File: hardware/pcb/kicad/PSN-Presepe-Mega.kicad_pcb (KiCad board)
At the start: 2 copper layers, 280 x 170 mm, 77 parts, among them J1 12V_IN, K1 G5Q-1_DC12, K10 G5Q-1_DC12, K11 G5Q-1_DC12, K12 G5Q-1_DC12, K13 G5Q-1_DC12, K14 G5Q-1_DC12, K15 G5Q-1_DC12, K16 G5Q-1_DC12, K2 G5Q-1_DC12, K3 G5Q-1_DC12, K4 G5Q-1_DC12, K5 G5Q-1_DC12, K6 G5Q-1_DC12, K7 G5Q-1_DC12, K8 G5Q-1_DC12, K9 G5Q-1_DC12, Q1 IRLZ44N_CIELO_R, Q2 IRLZ44N_CIELO_G, Q3 IRLZ44N_CIELO_B, Q4 IRLZ44N_TRAM_R, Q5 IRLZ44N_TRAM_G, Q6 IRLZ44N_TRAM_B, Q7 IRLZ44N_ALBA_R, Q8 IRLZ44N_ALBA_G, Q9 IRLZ44N_ALBA_B, U1 ULN2803C, U2 ULN2803C

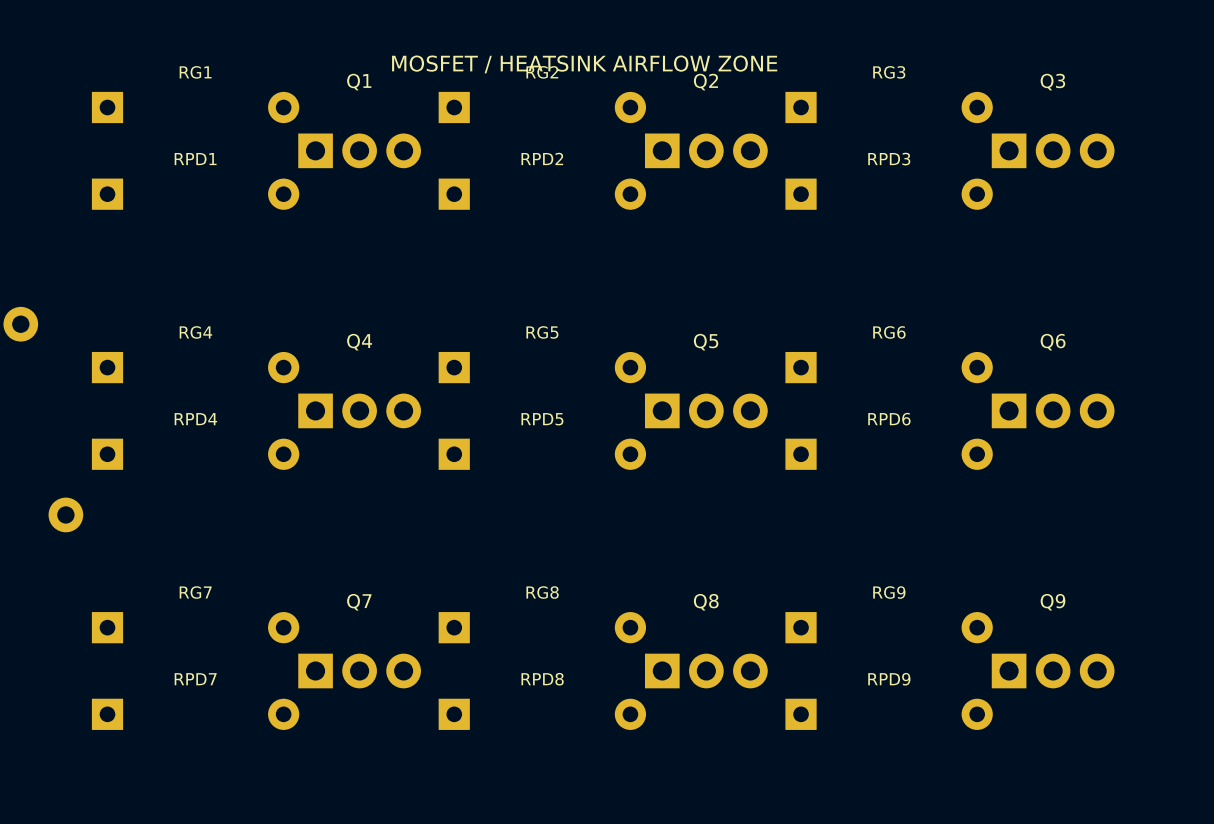
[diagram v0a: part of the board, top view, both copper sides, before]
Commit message: Route validated local MOSFET gate and ground network
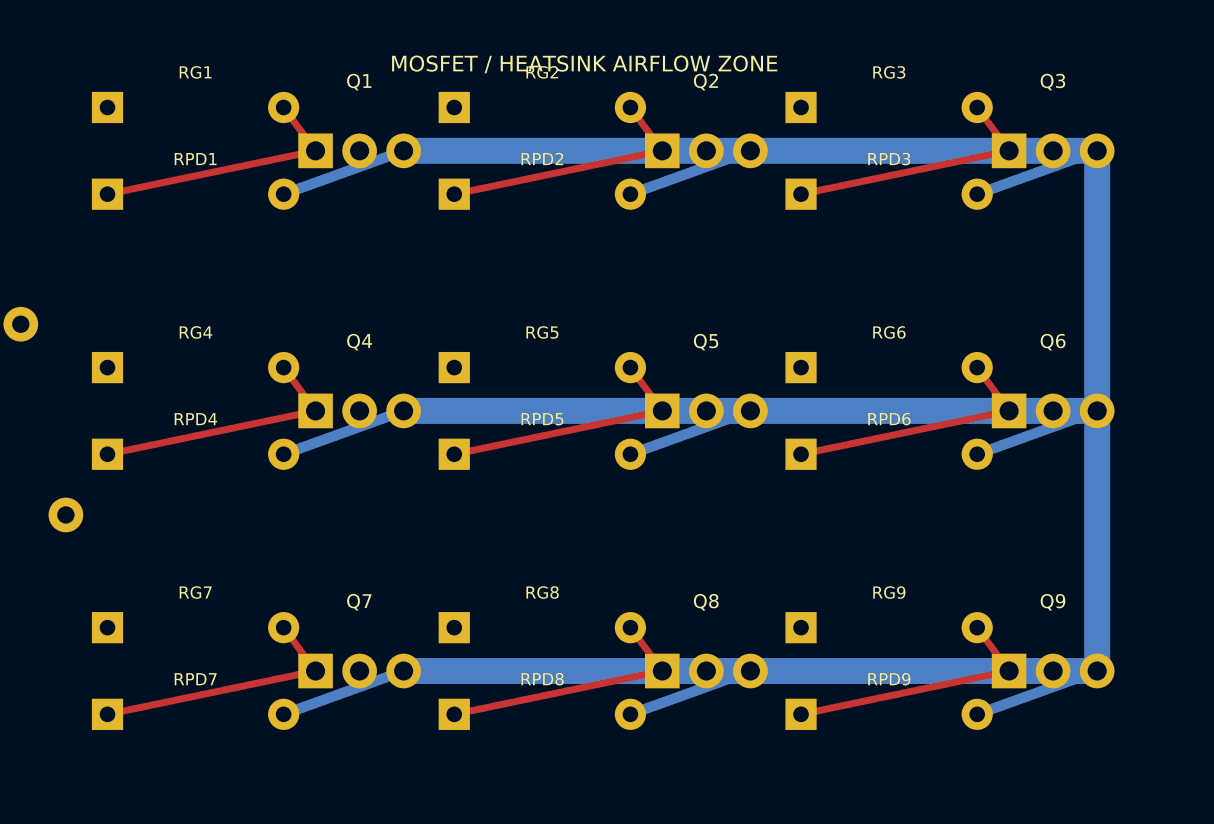
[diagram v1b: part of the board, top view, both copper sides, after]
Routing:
- net GND: track 0.00 -> 216.2 mm
- net GATE_Q9: track 0.00 -> 15.4 mm
- net GATE_Q8: track 0.00 -> 15.4 mm
- net GATE_Q7: track 0.00 -> 15.4 mm
- net GATE_Q6: track 0.00 -> 15.4 mm
- net GATE_Q5: track 0.00 -> 15.4 mm
- net GATE_Q4: track 0.00 -> 15.4 mm
- net GATE_Q3: track 0.00 -> 15.4 mm
- net GATE_Q2: track 0.00 -> 15.4 mm
- net GATE_Q1: track 0.00 -> 15.4 mm
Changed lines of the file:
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@@
   (gr_text "ALL TERMINAL WIRE ENTRY OUTWARD" (at 160 188) (layer "F.SilkS") (effects (font (size 0.9 0.9) (thickness 0.16))))
   (gr_text "MOSFET / HEATSINK AIRFLOW ZONE" (at 85.5 130) (layer "F.SilkS") (effects (font (size 0.9 0.9) (thickness 0.16))))
+  (segment (start 68.16 132.5) (end 70 135) (width 0.4) (layer "F.Cu") (net 63))
+  (segment (start 70 135) (end 58 137.5) (width 0.4) (layer "F.Cu") (net 63))
+  (segment (start 68.16 137.5) (end 75.08 135) (width 0.6) (layer "B.Cu") (net 1))
+  (segment (start 88.16 132.5) (end 90 135) (width 0.4) (layer "F.Cu") (net 64))
+  (segment (start 90 135) (end 78 137.5) (width 0.4) (layer "F.Cu") (net 64))
+  (segment (start 88.16 137.5) (end 95.08 135) (width 0.6) (layer "B.Cu") (net 1))
+  (segment (start 108.16 132.5) (end 110 135) (width 0.4) (layer "F.Cu") (net 65))
+  (segment (start 110 135) (end 98 137.5) (width 0.4) (layer "F.Cu") (net 65))
+  (segment (start 108.16 137.5) (end 115.08 135) (width 0.6) (layer "B.Cu") (net 1))
+  (segment (start 68.16 147.5) (end 70 150) (width 0.4) (layer "F.Cu") (net 66))
+  (segment (start 70 150) (end 58 152.5) (width 0.4) (layer "F.Cu") (net 66))
+  (segment (start 68.16 152.5) (end 75.08 150) (width 0.6) (layer "B.Cu") (net 1))
+  (segment (start 88.16 147.5) (end 90 150) (width 0.4) (layer "F.Cu") (net 67))
+  (segment (start 90 150) (end 78 152.5) (width 0.4) (layer "F.Cu") (net 67))
+  (segment (start 88.16 152.5) (end 95.08 150) (width 0.6) (layer "B.Cu") (net 1))
+  (segment (start 108.16 147.5) (end 110 150) (width 0.4) (layer "F.Cu") (net 68))
+  (segment (start 110 150) (end 98 152.5) (width 0.4) (layer "F.Cu") (net 68))
+  (segment (start 108.16 152.5) (end 115.08 150) (width 0.6) (layer "B.Cu") (net 1))
+  (segment (start 68.16 162.5) (end 70 165) (width 0.4) (layer "F.Cu") (net 69))
+  (segment (start 70 165) (end 58 167.5) (width 0.4) (layer "F.Cu") (net 69))
+  (segment (start 68.16 167.5) (end 75.08 165) (width 0.6) (layer "B.Cu") (net 1))
+  (segment (start 88.16 162.5) (end 90 165) (width 0.4) (layer "F.Cu") (net 70))
+  (segment (start 90 165) (end 78 167.5) (width 0.4) (layer "F.Cu") (net 70))
+  (segment (start 88.16 167.5) (end 95.08 165) (width 0.6) (layer "B.Cu") (net 1))
+  (segment (start 108.16 162.5) (end 110 165) (width 0.4) (layer "F.Cu") (net 71))
+  (segment (start 110 165) (end 98 167.5) (width 0.4) (layer "F.Cu") (net 71))
+  (segment (start 108.16 167.5) (end 115.08 165) (width 0.6) (layer "B.Cu") (net 1))
+  (segment (start 75.08 135) (end 115.08 135) (width 1.5) (layer "B.Cu") (net 1))
+  (segment (start 75.08 150) (end 115.08 150) (width 1.5) (layer "B.Cu") (net 1))
+  (segment (start 75.08 165) (end 115.08 165) (width 1.5) (layer "B.Cu") (net 1))
+  (segment (start 115.08 135) (end 115.08 165) (width 1.5) (layer "B.Cu") (net 1))
 )

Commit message: Route 12V ground and relay coil power
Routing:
- net +12V: track 0.00 -> 555.1 mm
- net GND: track 216.2 -> 445.7 mm
- net RELAY16_COIL_LOW: track 0.00 -> 195.2 mm
- net RELAY8_COIL_LOW: track 0.00 -> 179.2 mm
- net RELAY15_COIL_LOW: track 0.00 -> 176.7 mm
- net RELAY7_COIL_LOW: track 0.00 -> 160.7 mm
- net RELAY14_COIL_LOW: track 0.00 -> 158.3 mm
- net RELAY6_COIL_LOW: track 0.00 -> 142.3 mm
- net RELAY13_COIL_LOW: track 0.00 -> 139.8 mm
- net RELAY5_COIL_LOW: track 0.00 -> 123.8 mm
- net RELAY12_COIL_LOW: track 0.00 -> 121.4 mm
- net RELAY4_COIL_LOW: track 0.00 -> 105.4 mm
- net RELAY11_COIL_LOW: track 0.00 -> 102.9 mm
- net RELAY3_COIL_LOW: track 0.00 -> 86.9 mm
- net RELAY10_COIL_LOW: track 0.00 -> 84.4 mm
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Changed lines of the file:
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@@
   (segment (start 75.08 165) (end 115.08 165) (width 1.5) (layer "B.Cu") (net 1))
   (segment (start 115.08 135) (end 115.08 165) (width 1.5) (layer "B.Cu") (net 1))
+  (segment (start 28 184) (end 28 120) (width 1.5) (layer "B.Cu") (net 2))
+  (segment (start 28 120) (end 73.72 120) (width 1.5) (layer "B.Cu") (net 2))
+  (segment (start 73.72 120) (end 73.72 89.46) (width 1.5) (layer "B.Cu") (net 2))
+  (segment (start 73.72 120) (end 126.16 120) (width 1.5) (layer "B.Cu") (net 2))
+  (segment (start 126.16 120) (end 126.16 112.32) (width 1.0) (layer "B.Cu") (net 2))
+  (segment (start 126.16 82.32) (end 126.16 112.32) (width 1.0) (layer "B.Cu") (net 2))
+  (segment (start 150 60) (end 276 60) (width 1.5) (layer "B.Cu") (net 2))
+  (segment (start 150 115) (end 276 115) (width 1.5) (layer "B.Cu") (net 2))
+  (segment (start 126.16 82.32) (end 134 82.32) (width 1.0) (layer "B.Cu") (net 2))
+  (segment (start 134 82.32) (end 134 60) (width 1.0) (layer "B.Cu") (net 2))
+  (segment (start 134 60) (end 150 60) (width 1.0) (layer "B.Cu") (net 2))
+  (segment (start 126.16 112.32) (end 134 112.32) (width 1.0) (layer "B.Cu") (net 2))
+  (segment (start 134 112.32) (end 134 115) (width 1.0) (layer "B.Cu") (net 2))
+  (segment (start 134 115) (end 150 115) (width 1.0) (layer "B.Cu") (net 2))
+  (segment (start 33.08 184) (end 33.08 176) (width 1.5) (layer "B.Cu") (net 1))
+  (segment (start 33.08 176) (end 120 176) (width 1.5) (layer "B.Cu") (net 1))
+  (segment (start 68.64 89.46) (end 68.64 118) (width 1.2) (layer "B.Cu") (net 1))
+  (segment (start 68.64 118) (end 120 118) (width 1.2) (layer "B.Cu") (net 1))
+  (segment (start 116 82.32) (end 120 82.32) (width 0.8) (layer "B.Cu") (net 1))
+  (segment (start 120 82.32) (end 120 118) (width 1.0) (layer "B.Cu") (net 1))
+  (segment (start 116 112.32) (end 120 112.32) (width 0.8) (layer "B.Cu") (net 1))
+  (segment (start 115.08 165) (end 115.08 176) (width 1.5) (layer "B.Cu") (net 1))
+  (segment (start 126.16 62) (end 130 62) (width 0.5) (layer "B.Cu") (net 36))
+  (segment (start 130 62) (end 130 85.5) (width 0.5) (layer "B.Cu") (net 36))
+  (segment (start 130 85.5) (end 142.38 85.5) (width 0.5) (layer "B.Cu") (net 36))
+  (segment (start 142.38 85.5) (end 142.38 75.24) (width 0.5) (layer "B.Cu") (net 36))
+  (segment (start 126.16 64.54) (end 130 64.54) (width 0.5) (layer "B.Cu") (net 37))
+  (segment (start 130 64.54) (end 130 87) (width 0.5) (layer "B.Cu") (net 37))
+  (segment (start 130 87) (end 160.38 87) (width 0.5) (layer "B.Cu") (net 37))
+  (segment (start 160.38 87) (end 160.38 75.24) (width 0.5) (layer "B.Cu") (net 37))
+  (segment (start 126.16 67.08) (end 130 67.08) (width 0.5) (layer "B.Cu") (net 38))
+  (segment (start 130 67.08) (end 130 88.5) (width 0.5) (layer "B.Cu") (net 38))
+  (segment (start 130 88.5) (end 178.38 88.5) (width 0.5) (layer "B.Cu") (net 38))
+  (segment (start 178.38 88.5) (end 178.38 75.24) (width 0.5) (layer "B.Cu") (net 38))
+  (segment (start 126.16 69.62) (end 130 69.62) (width 0.5) (layer "B.Cu") (net 39))
+  (segment (start 130 69.62) (end 130 90) (width 0.5) (layer "B.Cu") (net 39))
+  (segment (start 130 90) (end 196.38 90) (width 0.5) (layer "B.Cu") (net 39))
+  (segment (start 196.38 90) (end 196.38 75.24) (width 0.5) (layer "B.Cu") (net 39))
+  (segment (start 126.16 72.16) (end 130 72.16) (width 0.5) (layer "B.Cu") (net 40))
+  (segment (start 130 72.16) (end 130 91.5) (width 0.5) (layer "B.Cu") (net 40))
+  (segment (start 130 91.5) (end 214.38 91.5) (width 0.5) (layer "B.Cu") (net 40))
+  (segment (start 214.38 91.5) (end 214.38 75.24) (width 0.5) (layer "B.Cu") (net 40))
+  (segment (start 126.16 74.7) (end 130 74.7) (width 0.5) (layer "B.Cu") (net 41))
+  (segment (start 130 74.7) (end 130 93) (width 0.5) (layer "B.Cu") (net 41))
+  (segment (start 130 93) (end 232.38 93) (width 0.5) (layer "B.Cu") (net 41))
+  (segment (start 232.38 93) (end 232.38 75.24) (width 0.5) (layer "B.Cu") (net 41))
+  (segment (start 126.16 77.24) (end 130 77.24) (width 0.5) (layer "B.Cu") (net 42))
+  (segment (start 130 77.24) (end 130 94.5) (width 0.5) (layer "B.Cu") (net 42))
+  (segment (start 130 94.5) (end 250.38 94.5) (width 0.5) (layer "B.Cu") (net 42))
+  (segment (start 250.38 94.5) (end 250.38 75.24) (width 0.5) (layer "B.Cu") (net 42))
+  (segment (start 126.16 79.78) (end 130 79.78) (width 0.5) (layer "B.Cu") (net 43))
+  (segment (start 130 79.78) (end 130 96) (width 0.5) (layer "B.Cu") (net 43))
+  (segment (start 130 96) (end 268.38 96) (width 0.5) (layer "B.Cu") (net 43))
+  (segment (start 268.38 96) (end 268.38 75.24) (width 0.5) (layer "B.Cu") (net 43))
+  (segment (start 126.16 92) (end 132 92) (width 0.5) (layer "B.Cu") (net 44))
+  (segment (start 132 92) (end 132 136) (width 0.5) (layer "B.Cu") (net 44))
+  (segment (start 132 136) (end 142.38 136) (width 0.5) (layer "B.Cu") (net 44))
+  (segment (start 142.38 136) (end 142.38 130.24) (width 0.5) (layer "B.Cu") (net 44))
+  (segment (start 126.16 94.54) (end 132 94.54) (width 0.5) (layer "B.Cu") (net 45))
+  (segment (start 132 94.54) (end 132 137.5) (width 0.5) (layer "B.Cu") (net 45))
+  (segment (start 132 137.5) (end 160.38 137.5) (width 0.5) (layer "B.Cu") (net 45))
+  (segment (start 160.38 137.5) (end 160.38 130.24) (width 0.5) (layer "B.Cu") (net 45))
+  (segment (start 126.16 97.08) (end 132 97.08) (width 0.5) (layer "B.Cu") (net 46))
+  (segment (start 132 97.08) (end 132 139) (width 0.5) (layer "B.Cu") (net 46))
+  (segment (start 132 139) (end 178.38 139) (width 0.5) (layer "B.Cu") (net 46))
+  (segment (start 178.38 139) (end 178.38 130.24) (width 0.5) (layer "B.Cu") (net 46))
+  (segment (start 126.16 99.62) (end 132 99.62) (width 0.5) (layer "B.Cu") (net 47))
+  (segment (start 132 99.62) (end 132 140.5) (width 0.5) (layer "B.Cu") (net 47))
+  (segment (start 132 140.5) (end 196.38 140.5) (width 0.5) (layer "B.Cu") (net 47))
+  (segment (start 196.38 140.5) (end 196.38 130.24) (width 0.5) (layer "B.Cu") (net 47))
+  (segment (start 126.16 102.16) (end 132 102.16) (width 0.5) (layer "B.Cu") (net 48))
+  (segment (start 132 102.16) (end 132 142) (width 0.5) (layer "B.Cu") (net 48))
+  (segment (start 132 142) (end 214.38 142) (width 0.5) (layer "B.Cu") (net 48))
+  (segment (start 214.38 142) (end 214.38 130.24) (width 0.5) (layer "B.Cu") (net 48))
+  (segment (start 126.16 104.7) (end 132 104.7) (width 0.5) (layer "B.Cu") (net 49))
+  (segment (start 132 104.7) (end 132 143.5) (width 0.5) (layer "B.Cu") (net 49))
+  (segment (start 132 143.5) (end 232.38 143.5) (width 0.5) (layer "B.Cu") (net 49))
+  (segment (start 232.38 143.5) (end 232.38 130.24) (width 0.5) (layer "B.Cu") (net 49))
+  (segment (start 126.16 107.24) (end 132 107.24) (width 0.5) (layer "B.Cu") (net 50))
+  (segment (start 132 107.24) (end 132 145) (width 0.5) (layer "B.Cu") (net 50))
+  (segment (start 132 145) (end 250.38 145) (width 0.5) (layer "B.Cu") (net 50))
+  (segment (start 250.38 145) (end 250.38 130.24) (width 0.5) (layer "B.Cu") (net 50))
+  (segment (start 126.16 109.78) (end 132 109.78) (width 0.5) (layer "B.Cu") (net 51))
+  (segment (start 132 109.78) (end 132 146.5) (width 0.5) (layer "B.Cu") (net 51))
+  (segment (start 132 146.5) (end 268.38 146.5) (width 0.5) (layer "B.Cu") (net 51))
+  (segment (start 268.38 146.5) (end 268.38 130.24) (width 0.5) (layer "B.Cu") (net 51))
 )
